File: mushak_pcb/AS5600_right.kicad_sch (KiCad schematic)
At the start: 7 parts, among them IC2 AS5600-ASOT

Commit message: Add footprints
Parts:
- C24, C25: footprint (none) -> Capacitor_SMD:C_0805_2012Metric
- IC2: footprint SOIC127P600X175-8N -> AS5600-ASOT:SOIC127P600X175-8N
- TP19: footprint (none) -> TestPoint:TestPoint_Pad_2.5x2.5mm
- TP21, TP22: footprint (none) -> TestPoint:TestPoint_Keystone_5019_Minature
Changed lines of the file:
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@@
     (property "Reference" "IC2" (id 0) (at 152.4 90.17 0))
     (property "Value" "AS5600-ASOT" (id 1) (at 152.4 92.71 0))
-    (property "Footprint" "SOIC127P600X175-8N" (id 2) (at 137.16 97.79 0)
+    (property "Footprint" "AS5600-ASOT:SOIC127P600X175-8N" (id 2) (at 137.16 97.79 0)
       (effects (font (size 1.27 1.27)) (justify left bottom) hide)
     )
@@
       (effects (font (size 1 1)) (justify left))
     )
-    (property "Footprint" "" (id 2) (at 173.99 105.41 0)
+    (property "Footprint" "TestPoint:TestPoint_Keystone_5019_Minature" (id 2) (at 173.99 105.41 0)
       (effects (font (size 1.27 1.27)) hide)
     )
@@
       (effects (font (size 1 1)) (justify left))
     )
-    (property "Footprint" "" (id 2) (at 173.99 107.95 0)
+    (property "Footprint" "TestPoint:TestPoint_Keystone_5019_Minature" (id 2) (at 173.99 107.95 0)
       (effects (font (size 1.27 1.27)) hide)
     )
@@
       (effects (font (size 1.27 1.27)) (justify right))
     )
-    (property "Footprint" "" (id 2) (at 116.84 113.03 0)
+    (property "Footprint" "TestPoint:TestPoint_Pad_2.5x2.5mm" (id 2) (at 116.84 113.03 0)
       (effects (font (size 1.27 1.27)) hide)
     )
@@
       (effects (font (size 1.27 1.27)) (justify left))
     )
-    (property "Footprint" "" (id 2) (at 127.9652 113.03 0)
+    (property "Footprint" "Capacitor_SMD:C_0805_2012Metric" (id 2) (at 127.9652 113.03 0)
       (effects (font (size 1.27 1.27)) hide)
     )
@@
       (effects (font (size 1.27 1.27)) (justify left))
     )
-    (property "Footprint" "" (id 2) (at 134.3152 113.03 0)
+    (property "Footprint" "Capacitor_SMD:C_0805_2012Metric" (id 2) (at 134.3152 113.03 0)
       (effects (font (size 1.27 1.27)) hide)
     )

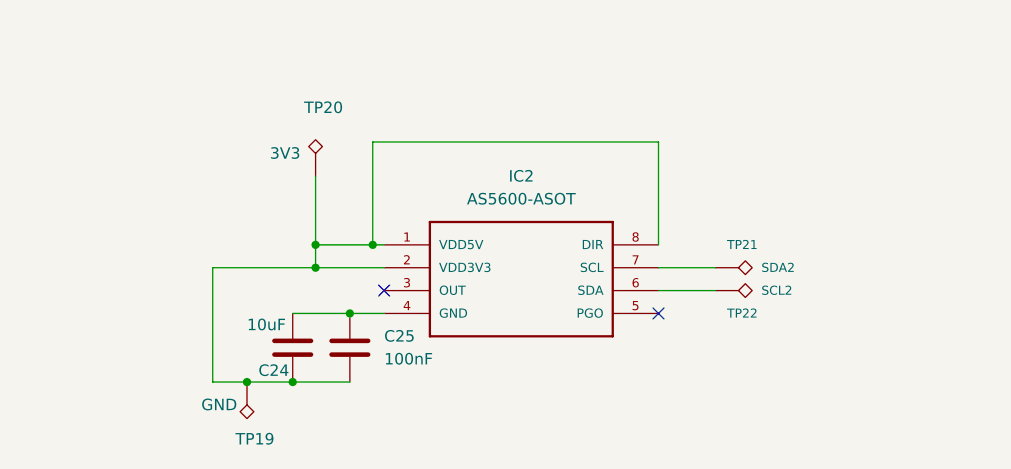
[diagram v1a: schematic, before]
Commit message: Update Schematics and footprints for sensors
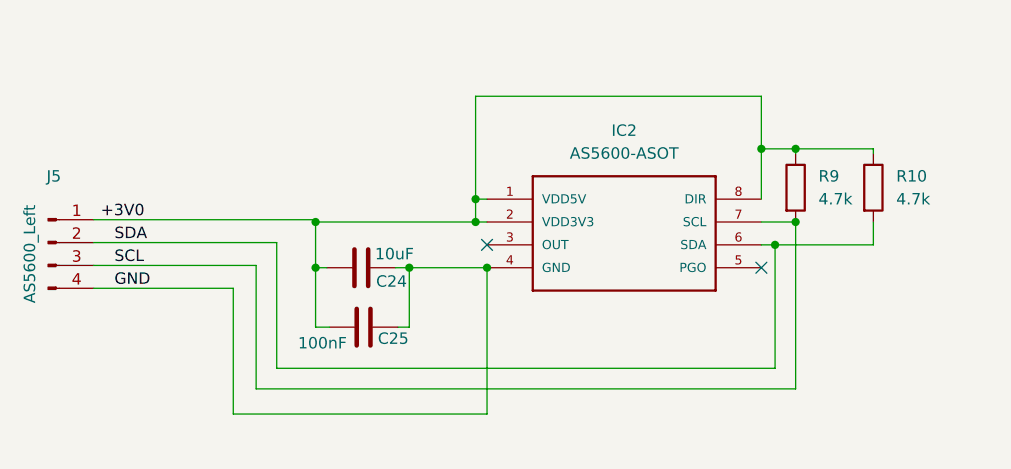
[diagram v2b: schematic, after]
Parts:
- removed TP19: GND, TestPoint:TestPoint_Pad_2.5x2.5mm, symbol Connector:TestPoint_Alt
- removed TP20: 3V3, TestPoint:TestPoint_Pad_3.0x3.0mm, symbol Connector:TestPoint_Alt
- removed TP21: SDA2, TestPoint:TestPoint_Keystone_5019_Minature, symbol Connector:TestPoint_Alt
- removed TP22: SCL2, TestPoint:TestPoint_Keystone_5019_Minature, symbol Connector:TestPoint_Alt
- added J5: AS5600_Left, mushak_mount_footprint:STAND_SLAVE_04, symbol Connector:Conn_01x04_Male
- added R10, R9: 4.7k, Resistor_SMD:R_0402_1005Metric, symbol Device:R
- C24, C25: footprint Capacitor_SMD:C_0805_2012Metric -> Capacitor_SMD:C_0402_1005Metric
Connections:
- net +3V0: now reaches IC2.1 (VDD5V), IC2.2 (VDD3V3), IC2.8 (DIR)
- net +3V0: now also C24.1, C25.1, J5.1 (Pin_1), R10.1, R9.1; no longer C24.2, C25.2
- net SDA: now reaches IC2.6 (SDA)
- net SDA: now also J5.2 (Pin_2), R10.2
- net SCL: now reaches IC2.7 (SCL)
- net SCL: now also J5.3 (Pin_3), R9.2
- new net GND: C24.2, C25.2, IC2.4 (GND), J5.4 (Pin_4)

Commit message: changed footprints of capacitors and resistors
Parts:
- C25: footprint Capacitor_SMD:C_0402_1005Metric -> Capacitor_SMD:C_0201_0603Metric
- R10, R9: footprint Resistor_SMD:R_0402_1005Metric -> Resistor_SMD:R_0201_0603Metric
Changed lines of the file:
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@@
       (effects (font (size 1.27 1.27)) (justify left))
     )
-    (property "Footprint" "Resistor_SMD:R_0402_1005Metric" (id 2) (at 181.102 91.44 90)
+    (property "Footprint" "Resistor_SMD:R_0201_0603Metric" (id 2) (at 181.102 91.44 90)
       (effects (font (size 1.27 1.27)) hide)
     )
@@
     (property "Reference" "C25" (id 0) (at 138.176 108.204 90))
     (property "Value" "100nF" (id 1) (at 130.302 108.712 90))
-    (property "Footprint" "Capacitor_SMD:C_0402_1005Metric" (id 2) (at 138.684 105.9688 0)
+    (property "Footprint" "Capacitor_SMD:C_0201_0603Metric" (id 2) (at 138.684 105.9688 0)
       (effects (font (size 1.27 1.27)) hide)
     )
@@
       (effects (font (size 1.27 1.27)) (justify left))
     )
-    (property "Footprint" "Resistor_SMD:R_0402_1005Metric" (id 2) (at 189.738 91.44 90)
+    (property "Footprint" "Resistor_SMD:R_0201_0603Metric" (id 2) (at 189.738 91.44 90)
       (effects (font (size 1.27 1.27)) hide)
     )

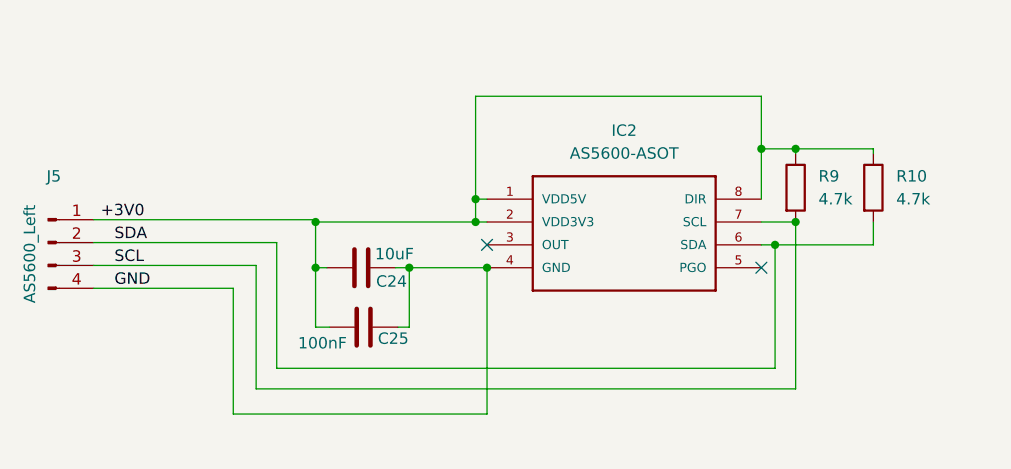
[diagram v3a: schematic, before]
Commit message: made draft pcb footprint placement
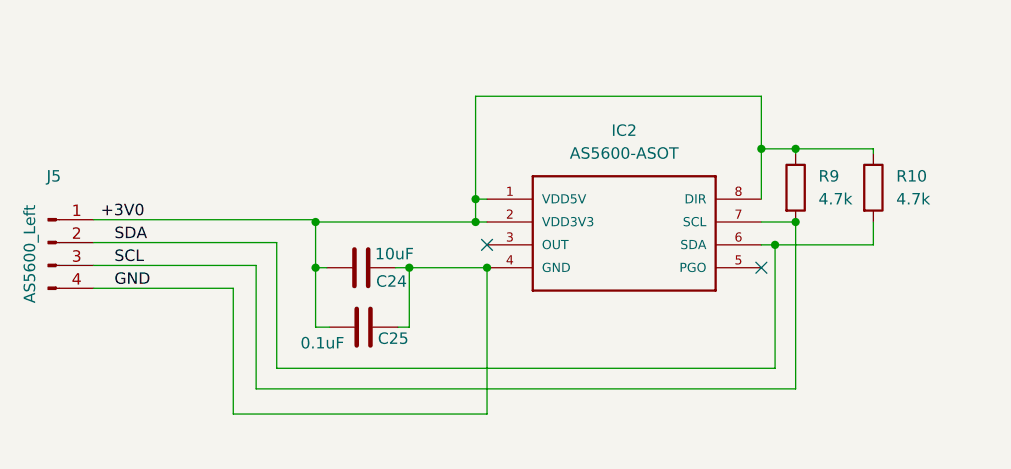
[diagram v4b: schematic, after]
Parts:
- C25: value 100nF -> 0.1uF
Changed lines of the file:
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@@
     (in_bom yes) (on_board yes)
     (property "Reference" "C25" (id 0) (at 138.176 108.204 90))
-    (property "Value" "100nF" (id 1) (at 130.302 108.712 90))
+    (property "Value" "0.1uF" (id 1) (at 130.302 108.712 90))
     (property "Footprint" "Capacitor_SMD:C_0201_0603Metric" (id 2) (at 138.684 105.9688 0)
       (effects (font (size 1.27 1.27)) hide)

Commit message: updated footprint for motors
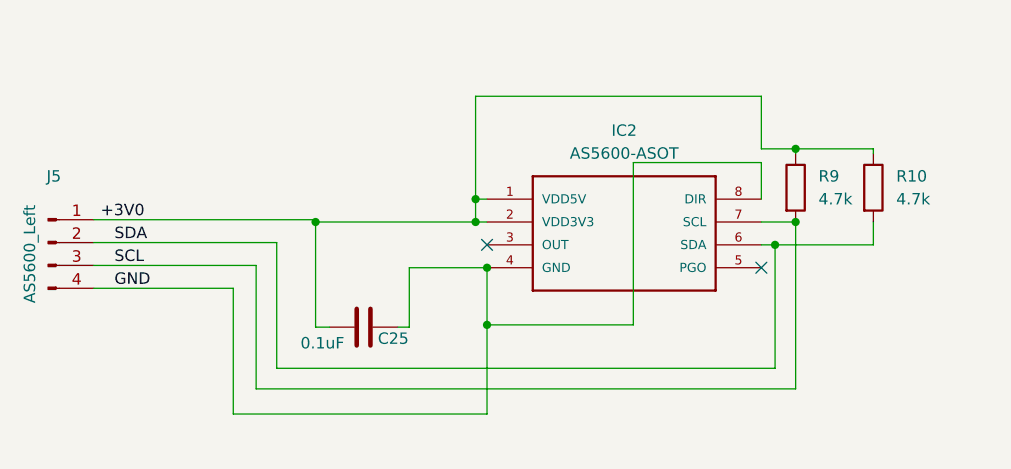
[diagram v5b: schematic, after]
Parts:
- removed C24: 10uF, Capacitor_SMD:C_0402_1005Metric, symbol Device:C
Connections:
- net +3V0: no longer IC2.8 (DIR)
- net GND: now also IC2.8 (DIR)
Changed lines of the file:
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@@
   (junction (at 129.54 95.25) (diameter 0) (color 0 0 0 0)
   )
-  (junction (at 129.54 100.33) (diameter 0) (color 0 0 0 0)
-  )
   (junction (at 147.32 95.25) (diameter 0) (color 0 0 0 0)
   )
   (junction (at 182.88 87.122) (diameter 0) (color 0 0 0 0)
   )
-  (junction (at 179.07 87.122) (diameter 0) (color 0 0 0 0)
+  (junction (at 148.59 106.68) (diameter 0) (color 0 0 0 0)
   )
   (junction (at 147.32 92.71) (diameter 0) (color 0 0 0 0)
   )
   (junction (at 180.594 97.79) (diameter 0) (color 0 0 0 0)
-  )
-  (junction (at 139.954 100.33) (diameter 0) (color 0 0 0 0)
   )
   (junction (at 182.88 95.25) (diameter 0) (color 0 0 0 0)
@@
     (stroke (width 0) (type default) (color 0 0 0 0))
   )
-  (wire (pts (xy 129.54 100.33) (xy 130.81 100.33))
-    (stroke (width 0) (type default) (color 0 0 0 0))
-  )
   (wire (pts (xy 182.88 87.63) (xy 182.88 87.122))
     (stroke (width 0) (type default) (color 0 0 0 0))
@@
     (stroke (width 0) (type default) (color 0 0 0 0))
   )
+  (wire (pts (xy 148.59 106.68) (xy 148.59 100.33))
+    (stroke (width 0) (type default) (color 0 0 0 0))
+  )
   (wire (pts (xy 139.954 106.934) (xy 139.954 100.33))
     (stroke (width 0) (type default) (color 0 0 0 0))
@@
     (stroke (width 0) (type default) (color 0 0 0 0))
   )
-  (wire (pts (xy 129.54 95.25) (xy 129.54 100.33))
+  (wire (pts (xy 129.54 95.25) (xy 129.54 106.934))
     (stroke (width 0) (type default) (color 0 0 0 0))
   )
@@
     (stroke (width 0) (type default) (color 0 0 0 0))
   )
-  (wire (pts (xy 148.59 116.586) (xy 148.59 100.33))
-    (stroke (width 0) (type default) (color 0 0 0 0))
-  )
-  (wire (pts (xy 129.54 106.934) (xy 129.54 100.33))
+  (wire (pts (xy 148.59 116.586) (xy 148.59 106.68))
+    (stroke (width 0) (type default) (color 0 0 0 0))
+  )
+  (wire (pts (xy 164.846 106.68) (xy 148.59 106.68))
+    (stroke (width 0) (type default) (color 0 0 0 0))
+  )
+  (wire (pts (xy 164.846 88.646) (xy 164.846 106.68))
     (stroke (width 0) (type default) (color 0 0 0 0))
   )
@@
     (stroke (width 0) (type default) (color 0 0 0 0))
   )
-  (wire (pts (xy 179.07 87.122) (xy 179.07 92.71))
+  (wire (pts (xy 179.07 88.646) (xy 164.846 88.646))
     (stroke (width 0) (type default) (color 0 0 0 0))
   )
@@
     (stroke (width 0) (type default) (color 0 0 0 0))
   )
+  (wire (pts (xy 179.07 92.71) (xy 179.07 88.646))
+    (stroke (width 0) (type default) (color 0 0 0 0))
+  )
   (wire (pts (xy 147.32 95.25) (xy 148.59 95.25))
     (stroke (width 0) (type default) (color 0 0 0 0))
@@
   )
   (wire (pts (xy 104.902 102.616) (xy 120.396 102.616))
-    (stroke (width 0) (type default) (color 0 0 0 0))
-  )
-  (wire (pts (xy 138.43 100.33) (xy 139.954 100.33))
     (stroke (width 0) (type default) (color 0 0 0 0))
   )
@@
     (pin "4")
   )
-  (symbol (lib_id "Device:C") (at 134.62 100.33 90) (unit 1)
-    (in_bom yes) (on_board yes)
-    (property "Reference" "C24" (id 0) (at 139.7 101.854 90)
-      (effects (font (size 1.27 1.27)) (justify left))
-    )
-    (property "Value" "10uF" (id 1) (at 140.462 98.806 90)
-      (effects (font (size 1.27 1.27)) (justify left))
-    )
-    (property "Footprint" "Capacitor_SMD:C_0402_1005Metric" (id 2) (at 138.43 99.3648 0)
-      (effects (font (size 1.27 1.27)) hide)
-    )
-    (property "Datasheet" "~" (id 3) (at 134.62 100.33 0)
-      (effects (font (size 1.27 1.27)) hide)
-    )
-    (pin "1")
-    (pin "2")
-  )
   (symbol (lib_id "Device:R") (at 191.516 91.44 0) (unit 1)

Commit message: corrected encoder and motor driver schematics
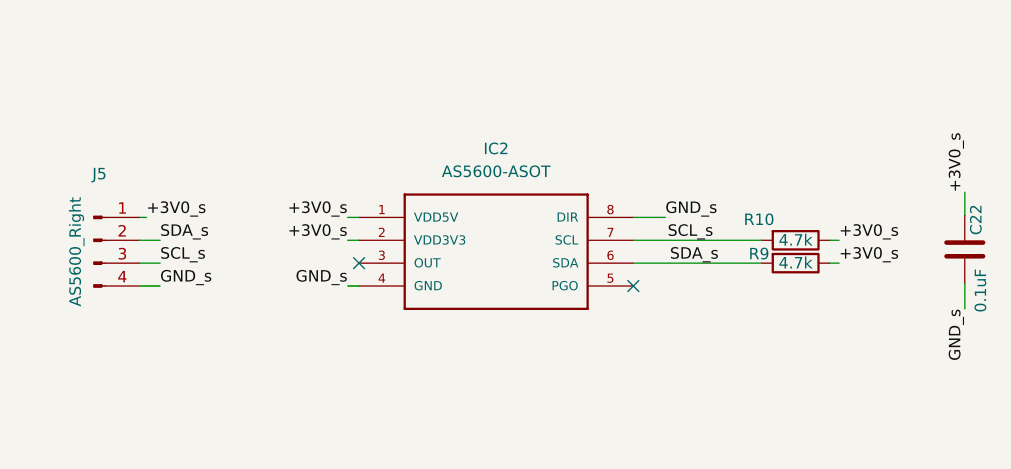
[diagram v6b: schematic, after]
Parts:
- removed C25: 0.1uF, Capacitor_SMD:C_0201_0603Metric, symbol Device:C
- added C22: 0.1uF, Capacitor_SMD:C_0402_1005Metric, symbol Device:C
- J5: value AS5600_Left -> AS5600_Right
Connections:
- net +3V0 renamed +3V0_s
- net +3V0_s: now also C22.2
- net GND renamed GND_s
- net GND_s: now also C22.1
- net SCL renamed SCL_s
- net SDA renamed SDA_s

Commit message: changed footprint of passive components
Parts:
- R10, R9: footprint Resistor_SMD:R_0201_0603Metric -> Resistor_SMD:R_0402_1005Metric
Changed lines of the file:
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@@
     (property "Reference" "R10" (id 0) (at 178.816 94.996 90))
     (property "Value" "4.7k" (id 1) (at 182.88 99.822 90))
-    (property "Footprint" "Resistor_SMD:R_0201_0603Metric" (id 2) (at 182.88 98.044 90)
+    (property "Footprint" "Resistor_SMD:R_0402_1005Metric" (id 2) (at 182.88 98.044 90)
       (effects (font (size 1.27 1.27)) hide)
     )
@@
     (property "Reference" "R9" (id 0) (at 178.816 98.806 90))
     (property "Value" "4.7k" (id 1) (at 182.88 97.282 90))
-    (property "Footprint" "Resistor_SMD:R_0201_0603Metric" (id 2) (at 182.88 95.504 90)
+    (property "Footprint" "Resistor_SMD:R_0402_1005Metric" (id 2) (at 182.88 95.504 90)
       (effects (font (size 1.27 1.27)) hide)
     )

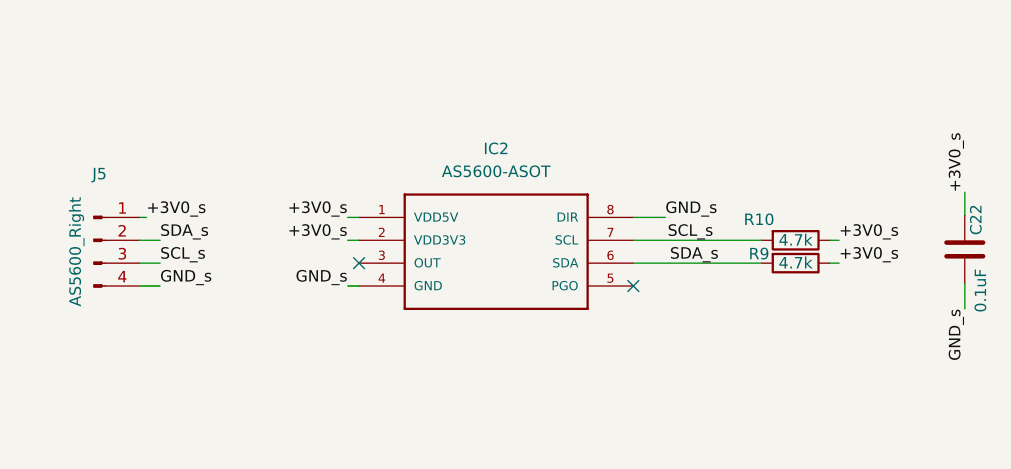
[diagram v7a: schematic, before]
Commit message: changed oscilattor placement
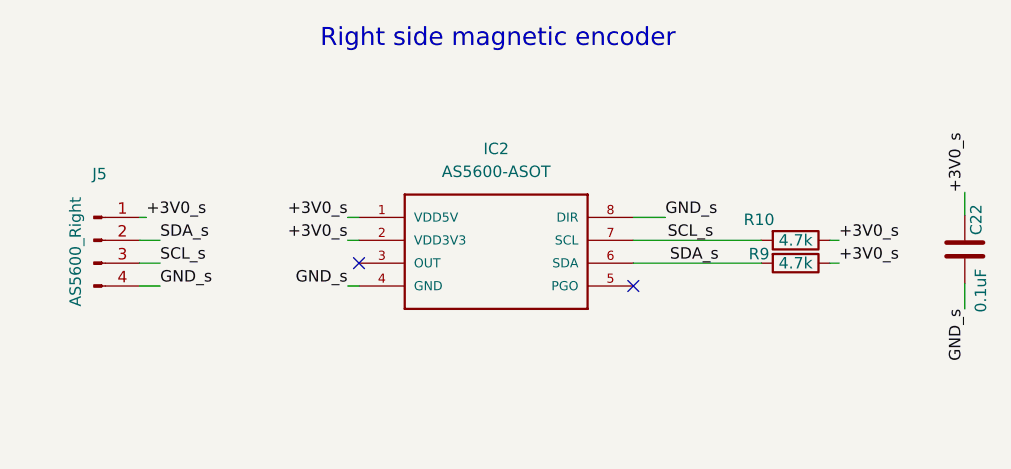
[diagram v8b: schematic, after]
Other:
- note added: "Right side magnetic encoder"
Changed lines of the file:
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@@
     (stroke (width 0) (type default) (color 0 0 0 0))
+  )
+  (text "Right side magnetic encoder" (at 130.048 76.073 0)
+    (effects (font (size 2 2)) (justify left bottom))
   )
   (label "+3V0_s" (at 201.676 91.948 90)
